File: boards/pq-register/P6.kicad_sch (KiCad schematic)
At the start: 93 parts, among them Q38 T1-N652, Q39 T1-N652, Q40 T1-N652, Q41 T1-N652, Q42 T1-N652, Q43 T1-N652, Q44 T1-N652, Q45 T1-N652, Q46 T1-N652, Q47 T1-N652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

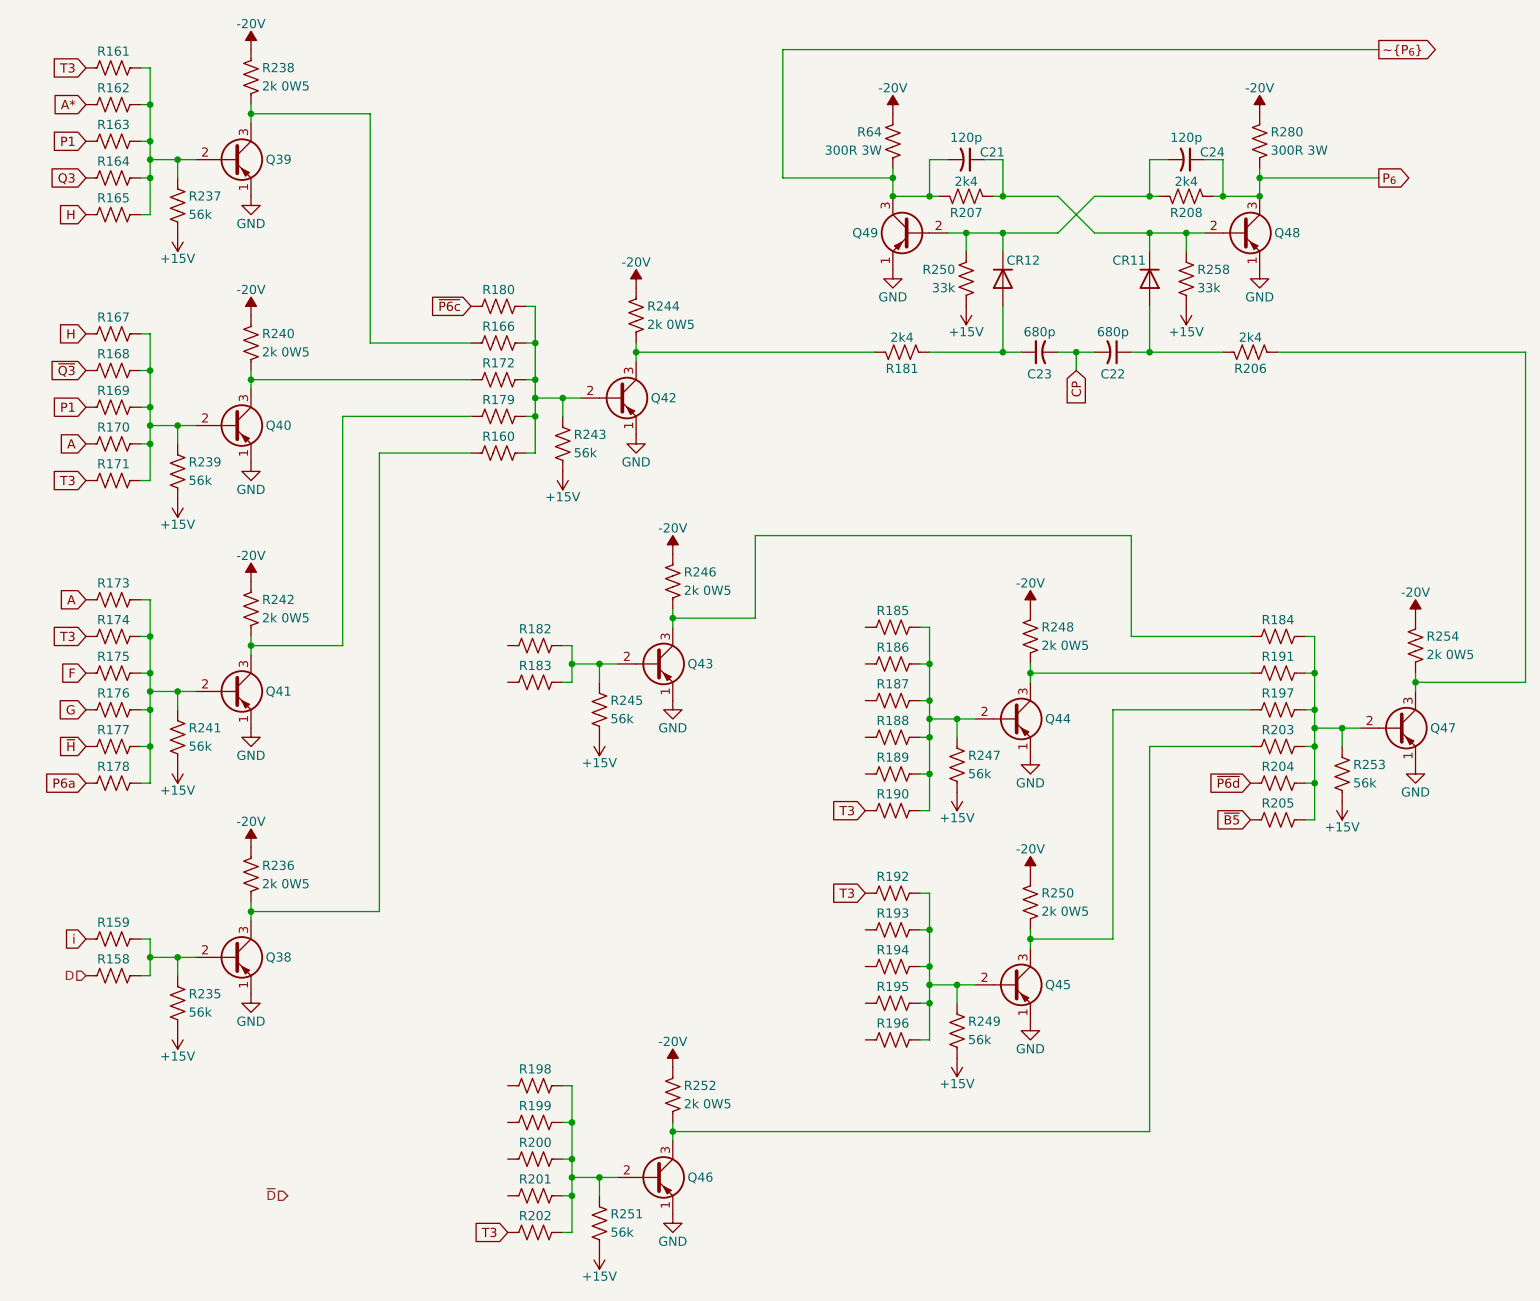
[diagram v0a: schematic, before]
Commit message: Run ERC and clean up P & Q Register board.
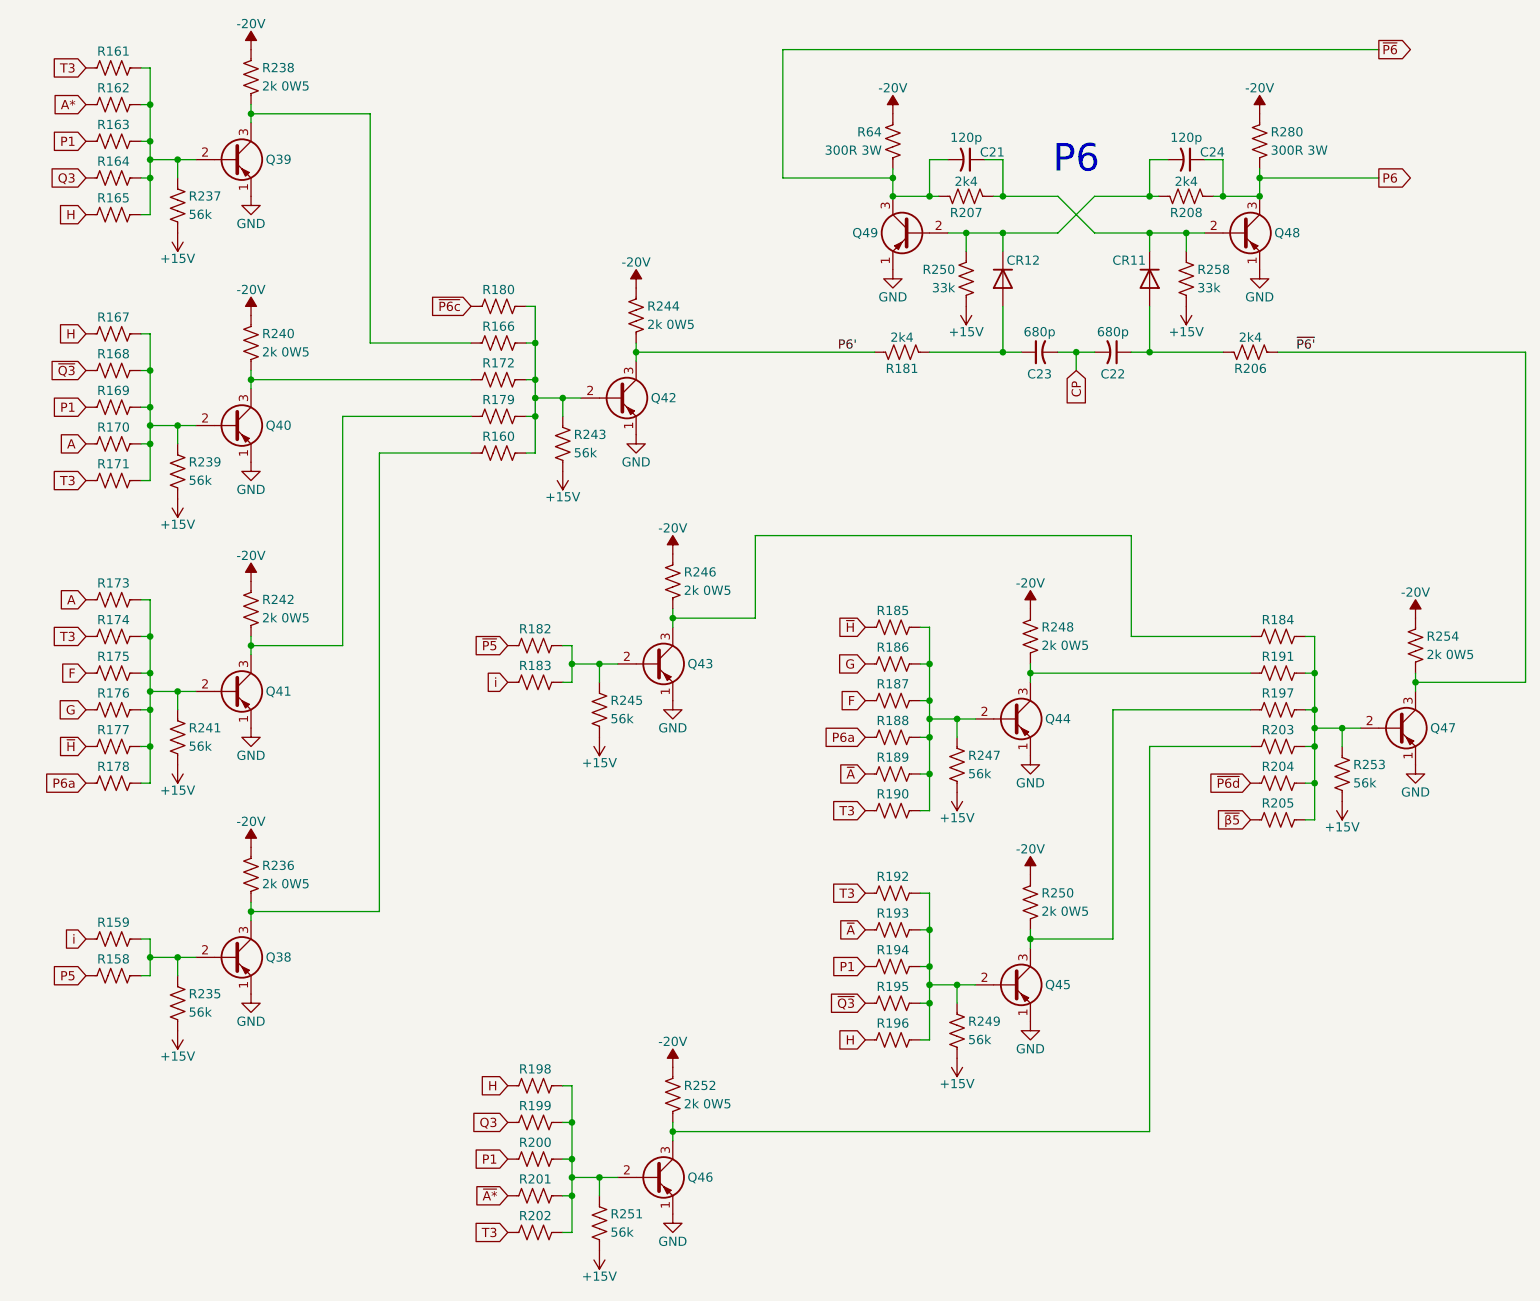
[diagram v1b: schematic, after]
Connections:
- net F: now also R187.1
- net G: now also R186.1
- net H: now also R196.1, R198.1
- net P1: now also R194.1, R200.1
- net P6a: now also R188.1
- net Q3: now also R199.1
- net i: now also R183.1
- net ~{H}: now also R185.1
- net ~{Q3}: now also R195.1
- net ~{P5}: now reaches R182.1
- net ~{P6'}: now reaches Q47.3 (C), R206.2, R254.2
- net ~{A*}: now reaches R201.1
- net ~{A}: now reaches R193.1
- net ~{A}: now also R189.1
- net P6': now reaches Q42.3 (C), R181.1, R244.2
- net D renamed P5
- net P_{6} renamed P6
- net ~{B5} renamed ~{β5}
- net ~{P_{6}} renamed ~{P6}
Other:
- note added: "P6"

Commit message: Add copyright information.
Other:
- company: (none) -> © 1962 General Precision; redrawn by Sam Hanes
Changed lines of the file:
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@@
 	(title_block
 		(title "LGP-21 P & Q Register Board")
+		(date "2026-06-15")
+		(rev "ESD 1060")
+		(company "© 1962 General Precision; redrawn by Sam Hanes")
+		(comment 1 "https://github.com/Elemecca/lgp21-docs")
 	)
 	(text "P6"
